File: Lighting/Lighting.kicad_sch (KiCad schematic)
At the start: 29 parts, among them J1 Frame connector, J10 Tool head connector, J11 X end stop, J12 Parts cooling fan, J13 Hotend Fan, J14 Thermistor, J15 Parts cooling fan, J16 Hot End fan, J17 LED Loom, J18 Motor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

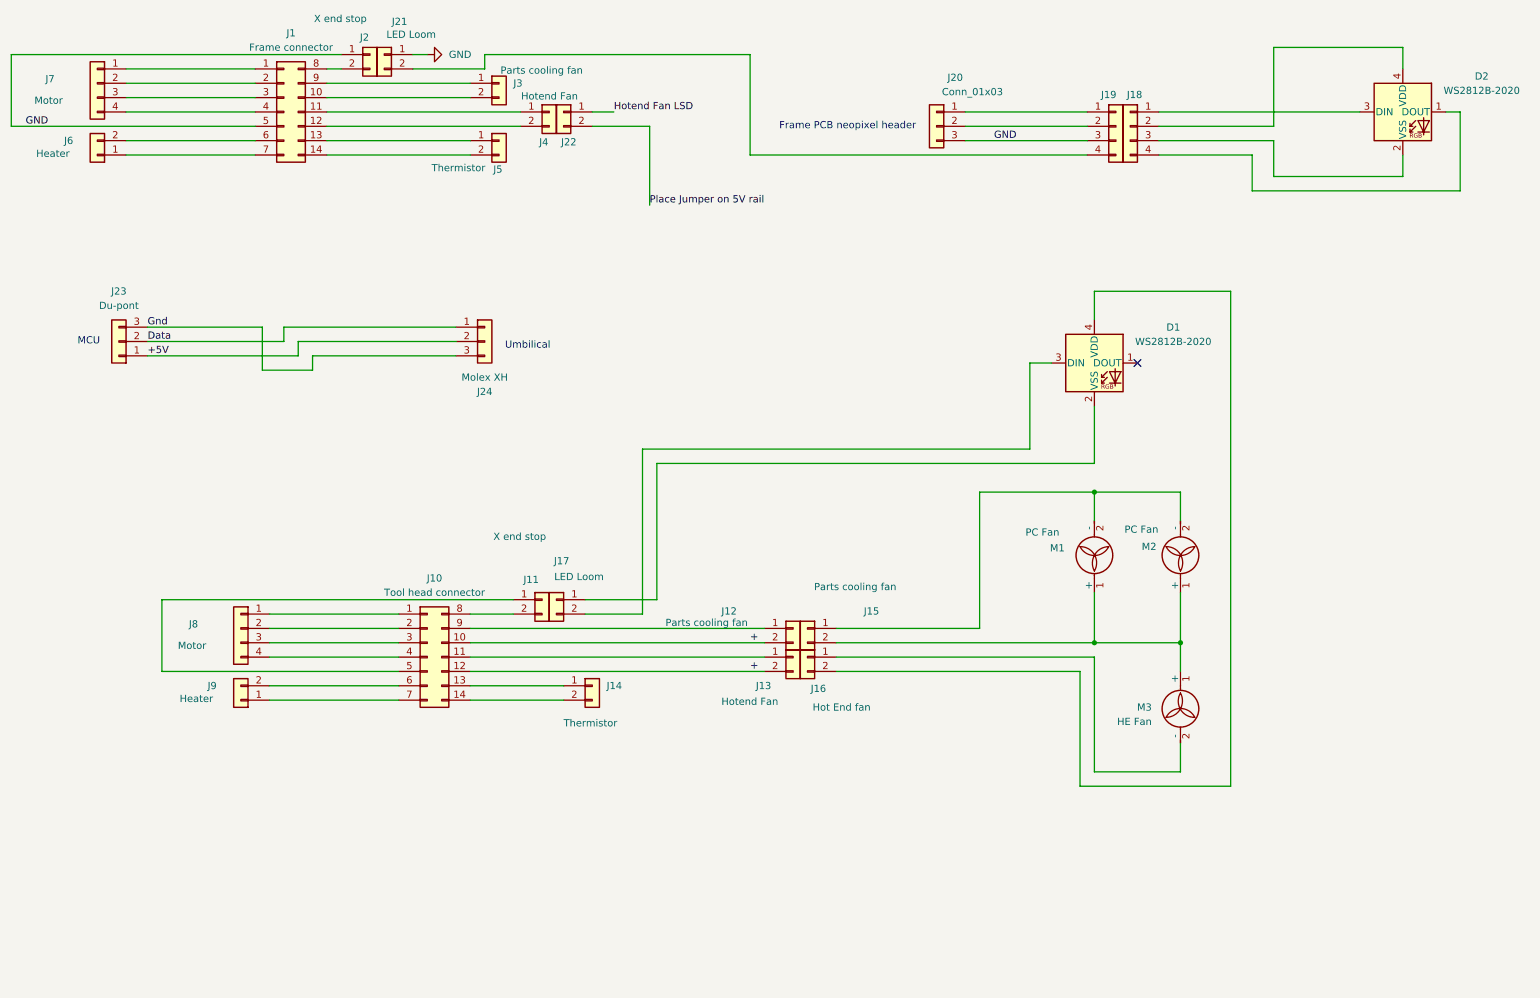
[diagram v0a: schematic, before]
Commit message: Complete update of new verson of spacer for LED PCB
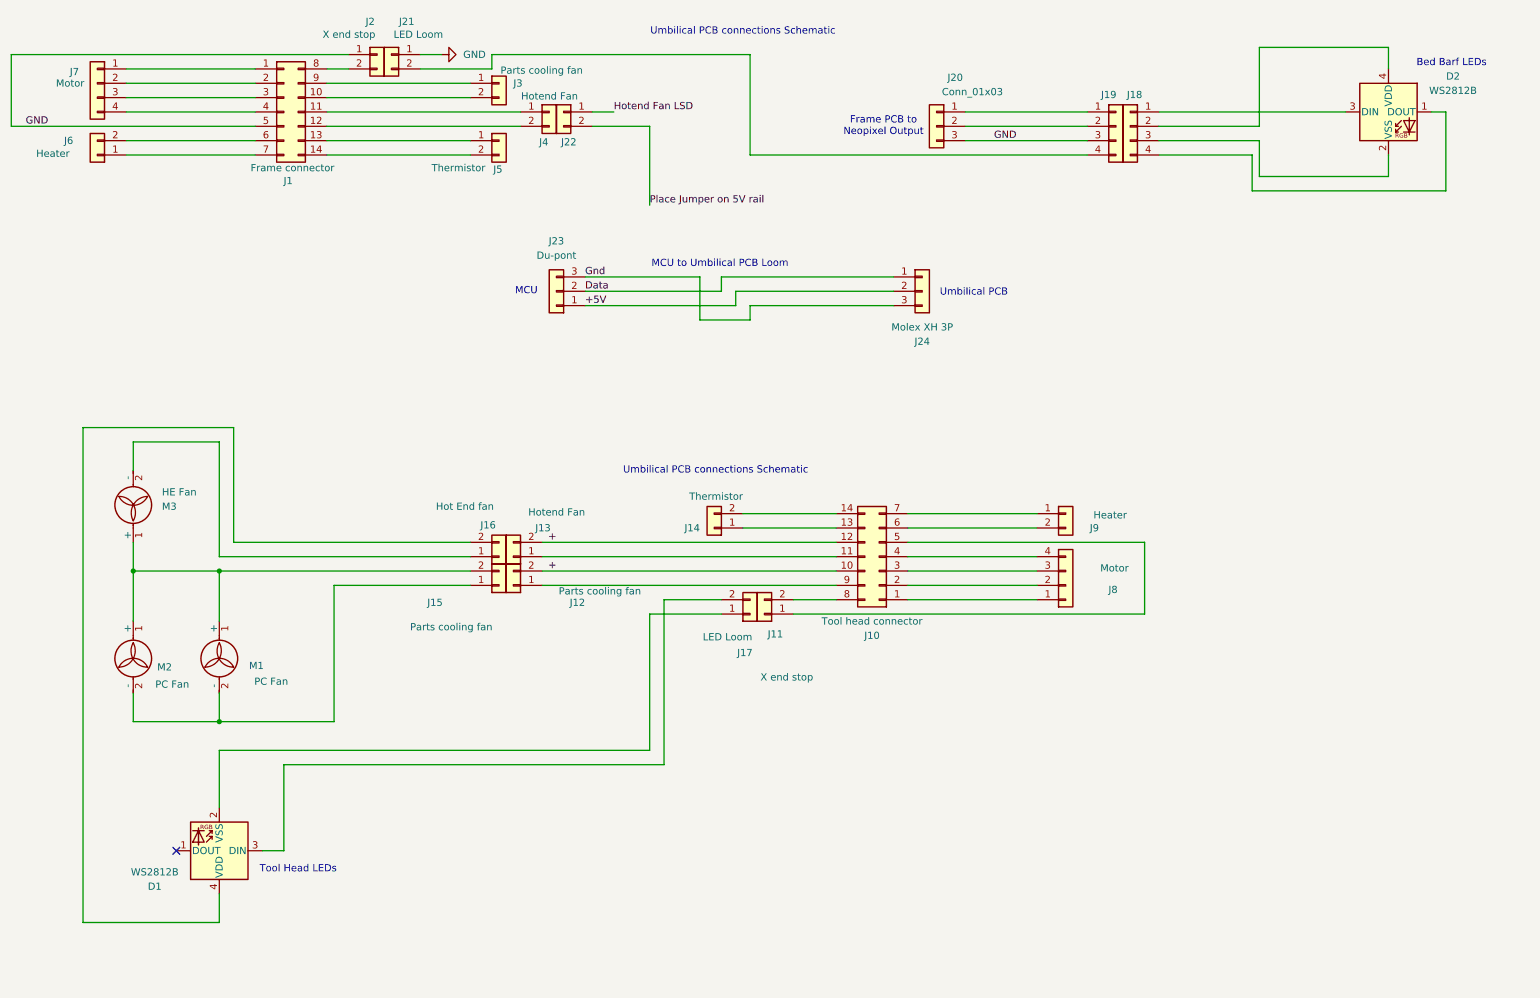
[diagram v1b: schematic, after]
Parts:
- D1, D2: value WS2812B-2020 -> WS2812B
- J24: value Molex XH -> Molex XH 3P
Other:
- note added: "Bed Barf LEDs"
- note added: "Frame PCB to Neopixel Output"
- note added: "MCU to Umbilical PCB Loom"
- note added: "Tool Head LEDs"
- note added: "Umbilical PCB"
- note added: "Umbilical PCB connections Schematic"
- note removed: "Frame PCB neopixel header"
- note removed: "Umbilical"
- moved on the sheet: D1, D2, J10, J11, J12, J13, J14, J15, J16, J17, J2, J21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

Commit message: Lighting schematic updated to make it easier to read
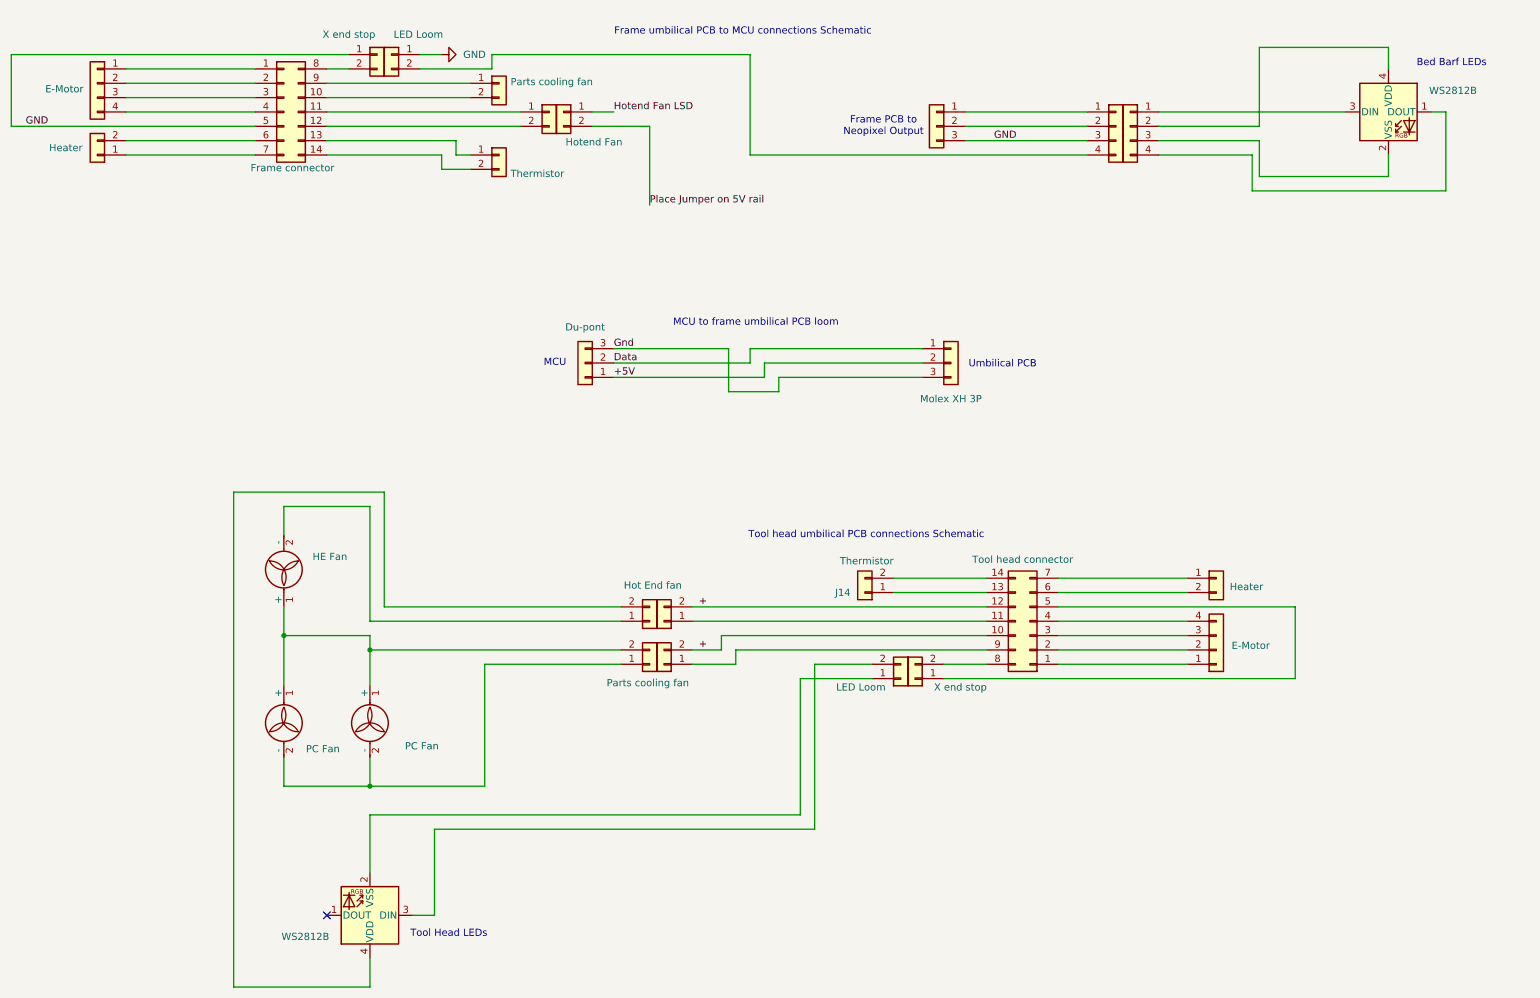
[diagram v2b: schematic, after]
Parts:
- J7, J8: value Motor -> E-Motor
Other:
- note added: "Frame umbilical PCB to MCU connections Schematic"
- note added: "MCU to frame umbilical PCB loom"
- note added: "Tool head umbilical PCB connections Schematic"
- note removed: "MCU to Umbilical PCB Loom"
- note removed: "Umbilical PCB connections Schematic"
- moved on the sheet: J14
